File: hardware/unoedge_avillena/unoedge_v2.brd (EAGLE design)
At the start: 73.6 x 49.2 mm, 47 parts, among them IC1 74HC574D, IC2 74HC574D, IC3 74HC574D, IC4 74HC574D, IC5 74HCT245DW, Q1 BSS123, Q2 BSS123, Q3 BSS123, Q4 BSS123, Q5 BSS123, Q6 BSS123, Q7 BSS123, Q8 BSS123

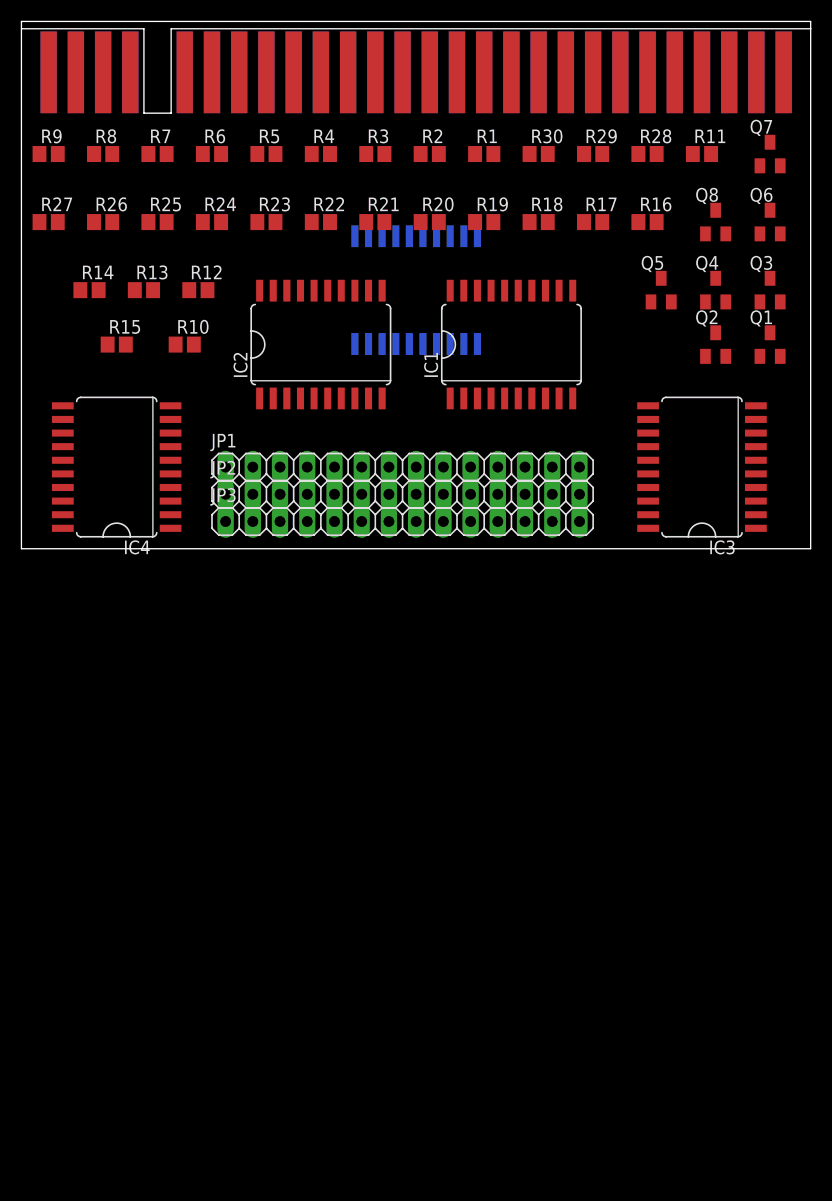
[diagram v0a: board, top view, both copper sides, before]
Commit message: 
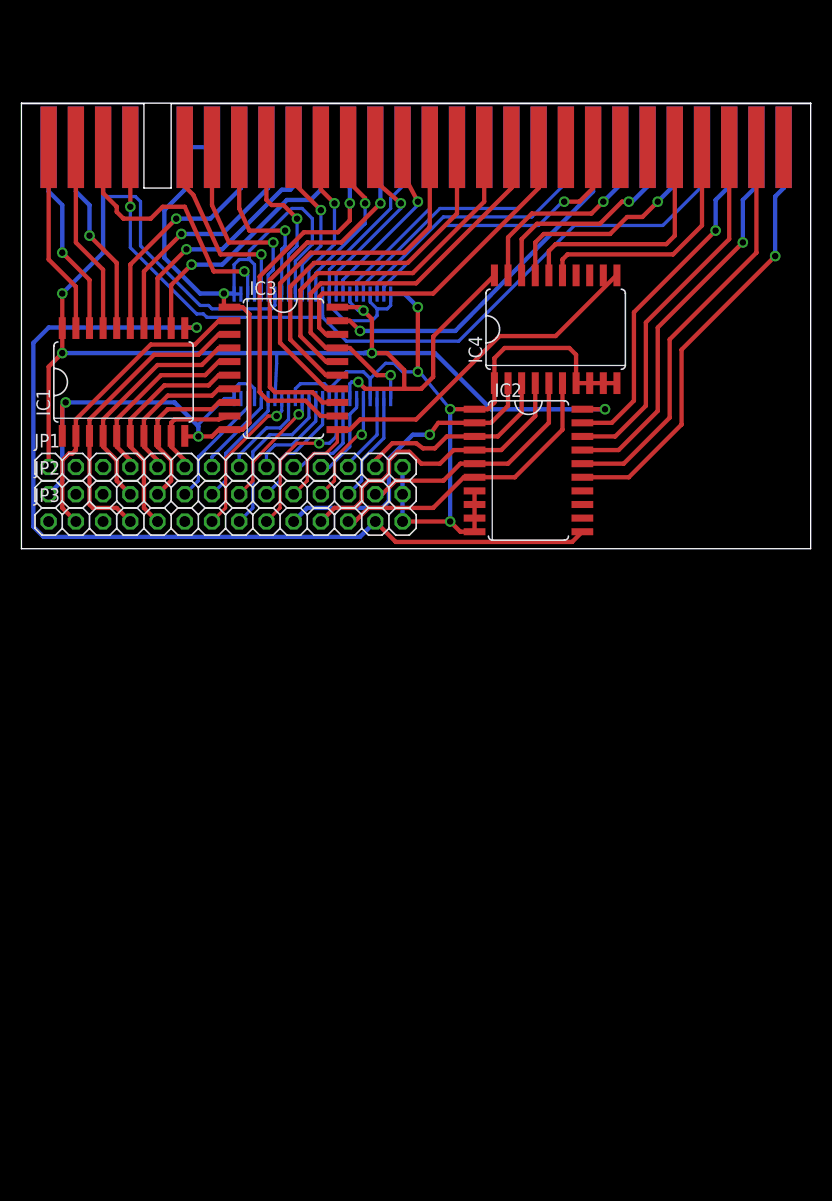
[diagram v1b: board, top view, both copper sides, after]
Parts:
- removed Q1, Q2, Q3, Q4, Q5, Q6, Q7, Q8: BSS123, transistor-small-signal:SOT23
- removed R1, R10, R11, R12, R13, R14, R15, R16, R17, R18, R19, R2, R20, R21, R22, R23, R24, R25, R26, R27, R28, R29, R3, R30, R4, R5, R6, R7, R8, R9: 10K, resistor:R0805
- IC5: value 74HCT245DW -> 74AC16245; device 74xx-eu:SO20W -> 74ac-logic:SSOP48DL
- JP1: value (none) -> fila1
- JP2: value (none) -> fila2
- JP3: value (none) -> fila3
- moved IC4 42.9 mm to (49.8, 20.5), turned to 0 degrees
- moved IC3 40.1 mm to (24.4, 16.8), turned to 270 degrees
- moved IC1 36.4 mm to (9.53, 15.6)
- moved IC2 22.7 mm to (47.3, 7.30), turned to 270 degrees
- moved JP1 16.5 mm to (19.1, 7.62)
- moved JP2 16.5 mm to (19.1, 5.08)
- moved JP3 16.5 mm to (19.1, 2.54)
- moved IC5 10.7 mm to (27.5, 18.9), turned to 0 degrees
- moved U$2 6.98 mm to (5.08, 34.9)
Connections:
- removed net +5V: JP1.1, R16.2, R18.2, R20.2, R22.2, R24.2, R26.2, R28.2, R30.2, U$2.P$30
- removed net EXT1: IC1.11, IC2.11, JP1.2
- removed net EXT2: IC3.11, IC4.11, JP2.2
- removed net ID0: IC5.2, Q1.3, R16.1
- removed net ID1: IC5.3, Q2.3, R18.1
- removed net ID2: IC5.4, Q3.3, R20.1
- removed net ID3: IC5.5, Q4.3, R22.1
- removed net ID4: IC5.6, Q5.3, R24.1
- removed net ID5: IC5.7, Q6.3, R26.1
- removed net ID6: IC5.8, Q7.3, R28.1
- removed net ID7: IC5.9, Q8.3, R30.1
- new net +3.3V: JP3.1
- new net EXT30: IC2.4, IC4.4, JP3.11
- new net EXT33: IC2.6, IC4.6, JP3.12
- new net EXT36: IC1.11, IC2.11, JP3.13
- net /BUSAK: now also IC2.19; no longer IC2.16
- net /BUSRQ: now also IC5.44; no longer R7.2
- net /HALT: now also IC3.14; no longer IC2.17
- net /INT: now also IC5.40; no longer R4.2
- net /IORQ: now also IC3.16; no longer IC4.18
- net /IORQULA: now also IC3.13; no longer IC4.15
- net /M1: now also IC4.16; no longer IC2.18
- net /MREQ: now also IC3.15; no longer IC4.19
- net /NMI: now also IC5.41; no longer R5.2
- net /RD: now also IC3.17; no longer IC4.16
- net /RESET: now also IC5.46; no longer R6.2
- net /RFSH: now also IC4.15; no longer IC2.19
- net /WAIT: now also IC5.47; no longer R8.2
- net /WR: now also IC3.18; no longer IC4.17
- net A0: now also IC1.14; no longer IC1.19
- net A1: now also IC1.13; no longer IC1.18
- net A10: now also IC2.16; no longer IC3.17
- net A11: now also IC2.15; no longer IC3.16
- net A12: now also IC1.16; no longer IC3.15
- net A13: now also IC1.17; no longer IC3.14
- net A14: now also IC1.18; no longer IC3.13
- net A15: now also IC1.19; no longer IC3.12
- net A2: now also IC1.12; no longer IC1.17
- net A3: now also IC3.12; no longer IC1.16
- net A4: now also IC4.17; no longer IC1.15
- net A5: now also IC4.18; no longer IC1.14
- net A6: now also IC4.19; no longer IC1.13
- net A7: now also IC3.19; no longer IC1.12
- net A8: now also IC2.18; no longer IC3.19
- net A9: now also IC2.17; no longer IC3.18
- net CKEXT: now also IC1.15; no longer IC2.15
- net D0: now also IC5.29; no longer IC5.18
- net D1: now also IC5.30; no longer IC5.17
- net D2: now also IC5.32; no longer IC5.16
- net D3: now also IC5.36; no longer IC5.15
- net D4: now also IC5.37; no longer IC5.14
- net D5: now also IC5.35; no longer IC5.13
- net D6: now also IC5.33; no longer IC5.12
- net D7: now also IC5.27; no longer IC5.11
- net EXT10: now also IC1.7, IC3.7; no longer IC1.3, IC3.3
- net EXT11: now also IC1.8, IC3.8; no longer IC2.5, IC4.5
- net EXT12: now also IC1.6, IC3.6; no longer Q3.2, R19.1
- net EXT13: now also IC1.9, IC3.9; no longer IC1.4, IC3.4
- net EXT14: now also IC5.22; no longer IC2.6, IC4.6
- net EXT15: no longer Q4.2, R21.1
- net EXT16: now also IC5.20; no longer IC1.5, IC3.5
- net EXT17: now also IC5.19; no longer R11.2, R4.1
- net EXT18: now also IC5.17; no longer Q5.2, R23.1
- net EXT19: now also IC5.16; no longer IC1.6, IC3.6
- net EXT20: now also IC5.14; no longer R12.2, R5.1
- net EXT21: now also IC5.13; no longer Q6.2, R25.1
- net EXT22: now also IC5.12; no longer IC1.7, IC3.7
- net EXT23: now also IC5.11; no longer R13.2, R6.1
- net EXT24: now also IC5.9; no longer Q7.2, R27.1
- net EXT25: now also IC5.8; no longer IC1.8, IC3.8
- net EXT26: now also IC3.11, IC4.11; no longer R14.2, R7.1
- net EXT27: now also IC2.2, IC4.2; no longer Q8.2, R29.1
- net EXT28: now also IC5.6; no longer IC1.9, IC3.9
- net EXT29: now also IC5.5; no longer R1.2, R8.1
- net EXT3: now also IC1.2, IC3.2; no longer Q1.2, R15.1
- net EXT31: now also IC5.3; no longer IC2.2, IC4.2
- net EXT32: now also IC5.2; no longer R2.2, R9.1
- net EXT35: now also IC2.5, IC4.5; no longer R10.1, R3.2
- net EXT7: now also IC1.5, IC3.5; no longer IC1.2, IC3.2
- net EXT8: now also IC1.4, IC3.4; no longer IC2.4, IC4.4
- net EXT9: now also IC1.3, IC3.3; no longer Q2.2, R17.1
- net GND: now also IC2.9, IC5.15, IC5.21, IC5.24, IC5.25, IC5.26, IC5.28, IC5.34, IC5.39, IC5.4, IC5.45, IC5.48; no longer IC5.19, R1.1, R11.1, R12.1, R13.1, R14.1, R2.1, R3.1
- net ROM1: now also IC5.38; no longer R9.2
- net ROM2: now also IC5.43; no longer R10.2
- net VCC: now also IC5.18, IC5.31, IC5.42, IC5.7, JP1.1, U$2.P$30; no longer IC5.20, JP3.1, Q1.1, Q2.1, Q3.1, Q4.1, Q5.1, Q6.1, Q7.1, Q8.1, R15.2, R17.2, R19.2, R21.2, R23.2, R25.2, R27.2, R29.2
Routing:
- net GND: track 0.00 -> 210.8 mm, vias 0 -> 7
- net VCC: track 0.00 -> 153.4 mm, vias 0 -> 6
- net EXT36: track 0.00 -> 87.5 mm, vias 0 -> 1
- net ROM1: track 0.00 -> 78.2 mm, vias 0 -> 1
- net /RD: track 0.00 -> 41.6 mm, vias 0 -> 1
- net A11: track 0.00 -> 41.1 mm, vias 0 -> 1
- net EXT26: track 0.00 -> 40.5 mm
- net A10: track 0.00 -> 38.5 mm
- net A9: track 0.00 -> 37.0 mm, vias 0 -> 1
- net A3: track 0.00 -> 36.4 mm, vias 0 -> 1
- net /HALT: track 0.00 -> 36.3 mm
- net /IORQULA: track 0.00 -> 35.6 mm, vias 0 -> 1
- net /MREQ: track 0.00 -> 35.3 mm
- net A8: track 0.00 -> 34.5 mm
- net /IORQ: track 0.00 -> 34.4 mm
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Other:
- board size 73.6 x 49.2 mm -> 73.6 x 41.6 mm

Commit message: planos de masa
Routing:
- added copper zone on layer 16, net GND
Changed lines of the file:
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@@
 <wire x1="2.54" y1="16.98625" x2="3.81" y2="18.25625" width="0.4064" layer="1"/>
 <via x="3.81" y="18.25625" extent="1-16" drill="0.6" shape="octagon"/>
-<wire x1="23.8125" y1="18.25625" x2="24.13" y2="18.25625" width="0" layer="19" extent="1-16"/>
 <wire x1="31.90875" y1="18.25625" x2="32.7025" y2="18.25625" width="0.4064" layer="16"/>
 <wire x1="32.7025" y1="18.25625" x2="38.57625" y2="18.25625" width="0.4064" layer="16"/>
@@
 <wire x1="10.63625" y1="32.86125" x2="7.77875" y2="32.86125" width="0.3048" layer="16"/>
 <wire x1="7.77875" y1="32.86125" x2="7.62" y2="32.7025" width="0.3048" layer="16"/>
-<wire x1="24.28875" y1="17.62125" x2="24.28875" y2="18.0975" width="0" layer="19" extent="1-16"/>
-<wire x1="24.28875" y1="18.0975" x2="24.13" y2="18.25625" width="0" layer="19" extent="1-16"/>
 <wire x1="16.66875" y1="22.70125" x2="17.4625" y2="22.70125" width="0.3048" layer="16"/>
 <wire x1="17.4625" y1="22.70125" x2="17.78" y2="22.38375" width="0.3048" layer="16"/>
@@
 <wire x1="21.2725" y1="27.78125" x2="21.2725" y2="27.14625" width="0.3048" layer="16"/>
 <wire x1="21.2725" y1="27.14625" x2="21.11375" y2="26.9875" width="0.3048" layer="16"/>
-<wire x1="21.74875" y1="14.9225" x2="22.225" y2="16.66875" width="0" layer="19" extent="1-16"/>
-<wire x1="22.225" y1="16.66875" x2="25.0825" y2="16.66875" width="0" layer="19" extent="1-16"/>
-<wire x1="25.0825" y1="16.66875" x2="25.55875" y2="14.9225" width="0" layer="19" extent="1-16"/>
 <contactref element="JP2" pad="1"/>
 <wire x1="2.54" y1="5.08" x2="3.81" y2="6.35" width="0.4064" layer="16"/>
 <wire x1="3.81" y1="6.35" x2="3.81" y2="13.335" width="0.4064" layer="16"/>
 <wire x1="3.81" y1="13.335" x2="4.1275" y2="13.6525" width="0.4064" layer="16"/>
+<polygon width="0.4064" layer="16">
+<vertex x="0.79375" y="33.17875"/>
+<vertex x="72.86625" y="33.17875"/>
+<vertex x="72.86625" y="0.3175"/>
+<vertex x="0.635" y="0.3175"/>
+<vertex x="0.635" y="33.17875"/>
+</polygon>
+<wire x1="28.73375" y1="26.035" x2="27.14625" y2="28.41625" width="0" layer="19" extent="16-16"/>
 </signal>
 <signal name="EXT7">

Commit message: Cambios propuestos por McLeod
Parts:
- added Q1, Q2, Q3, Q4: BSS123, transistor-small-signal:SOT23
- added R1, R2, R3, R4, R5, R6, R7: (no value), rcl:M0805
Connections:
- removed net ROM1: IC5.38, U$2.P$4, U$2.P$51
- removed net ROM2: IC5.43, U$2.P$41
- new net /Y: IC1.15, U$2.P$42
- new net EXT1: JP1.2, Q4.1
- new net ROMCS: IC5.43, U$2.P$4, U$2.P$41, U$2.P$51
- net +3.3V: now also Q1.1, Q2.1, Q3.1, R1.2, R2.2, R3.2
- net /INT: now also Q2.3, R5.1; no longer IC5.40
- net /IORQULA: now also Q3.3, R6.1; no longer IC3.13
- net /RD: no longer IC5.1
- net /RESET: now also Q1.3, R4.1; no longer IC5.46
- net CKEXT: now also Q4.3, R7.1; no longer IC1.15
- net D0: now also IC5.27; no longer IC5.29
- net D1: now also IC5.29; no longer IC5.30
- net D2: now also IC5.30; no longer IC5.32
- net D3: now also IC5.35; no longer IC5.36
- net D4: now also IC5.36; no longer IC5.37
- net D5: now also IC5.33; no longer IC5.35
- net D6: now also IC5.32; no longer IC5.33
- net D7: now also IC5.26; no longer IC5.27
- net EXT11: now also Q3.2, R3.1; no longer IC3.8
- net EXT14: now also IC5.24; no longer IC5.22
- net EXT15: now also IC1.11, IC2.11, IC3.11, IC4.11
- net EXT16: now also IC5.23; no longer IC5.20
- net EXT17: now also IC5.22; no longer IC5.19
- net EXT18: now also IC5.20; no longer IC5.17
- net EXT19: now also IC5.19; no longer IC5.16
- net EXT20: now also IC5.17; no longer IC5.14
- net EXT21: now also IC5.16; no longer IC5.13
- net EXT22: now also IC5.14; no longer IC5.12
- net EXT23: now also IC5.13; no longer IC5.11
- net EXT24: now also Q2.2, R2.1; no longer IC5.9
- net EXT26: now also IC3.1, IC4.1; no longer IC3.11, IC4.11
- net EXT31: now also Q1.2, R1.1; no longer IC5.3
- net EXT36: now also IC1.1, IC2.1; no longer IC1.11, IC2.11
- net GND: now also IC5.1, Q4.2; no longer IC1.1, IC2.1, IC3.1, IC4.1, IC5.24, IC5.26
- net VCC: now also R4.2, R5.2, R6.2, R7.2
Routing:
- net ROMCS: track 0.00 -> 81.4 mm, vias 0 -> 1
- net ROM1: track 78.2 -> 0.00 mm, vias 1 -> 0
- net EXT26: track 40.5 -> 9.91 mm
- net GND: track 210.8 -> 192.2 mm
- net ROM2: track 16.5 -> 0.00 mm
- net CKEXT: track 23.1 -> 17.2 mm
- net EXT24: track 15.9 -> 12.4 mm
- net EXT31: track 7.51 -> 4.13 mm
- net D0: track 18.4 -> 16.2 mm
- net /RD: track 41.6 -> 39.4 mm
- net D2: track 17.4 -> 15.3 mm
- net /INT: track 17.3 -> 15.3 mm
- net D1: track 18.4 -> 16.7 mm
- net A3: track 36.4 -> 34.8 mm
- net D5: track 15.5 -> 13.9 mm
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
